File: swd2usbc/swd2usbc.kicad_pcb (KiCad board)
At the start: 4 copper layers, 18.3 x 16 mm, 16 parts, among them J1 USB_C_Receptacle_USB2.0, J2 Conn_ARM_JTAG_SWD_10, P1 USB_C_Plug, U1 ATtiny24-20M

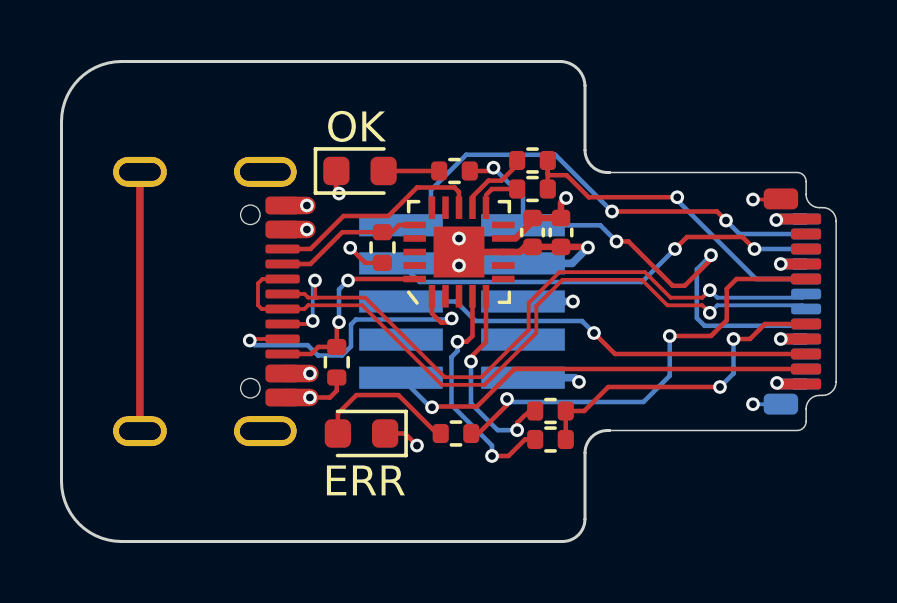
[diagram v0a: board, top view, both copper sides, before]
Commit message: Various fixes while ordering from JLCPCB
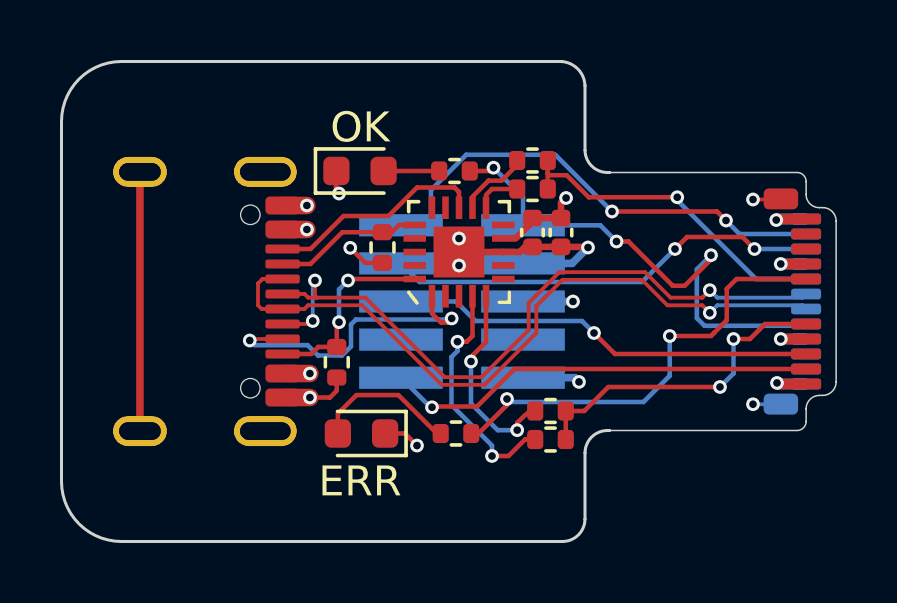
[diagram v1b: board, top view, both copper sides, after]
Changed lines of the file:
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@@
 	(generator_version "8.0")
 	(general
-		(thickness 0.8208)
+		(thickness 0.8)
 		(legacy_teardrops no)
 	)
@@
 			(layer "dielectric 1"
 				(type "prepreg")
-				(thickness 0.1 locked)
+				(thickness 0.1)
 				(material "FR408-HR")
 				(epsilon_r 3.69)
@@
 			(layer "dielectric 2"
 				(type "core")
-				(thickness 0.465)
+				(thickness 0.4442)
 				(material "FR408-HR")
 				(epsilon_r 3.69)
@@
 			(layer "dielectric 3"
 				(type "prepreg")
-				(thickness 0.1 locked)
+				(thickness 0.1)
 				(material "FR408-HR")
 				(epsilon_r 3.69)
@@
 			)
 		)
-		(property "LCSC" "C72043"
+		(property "LCSC" "C965804"
 			(at 0 0 0)
 			(unlocked yes)
@@
 			)
 		)
-		(property "LCSC" "C220282"
+		(property "LCSC" "C617902"
 			(at 0 0 0)
 			(layer "F.SilkS")
@@
 	)
 	(gr_text "ERR"
-		(at 165.35 73.5 0)
+		(at 165.2 73.5 0)
 		(layer "F.SilkS")
 		(effects
@@
 	)
 	(gr_text "OK"
-		(at 165.05 61.7 0)
+		(at 165.2 61.7 0)
 		(layer "F.SilkS")
 		(effects

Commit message: Should have checked my footprints...
USB-C plug footprint was incorrect. I had fixed it in the library but forgot to update it in the project.........
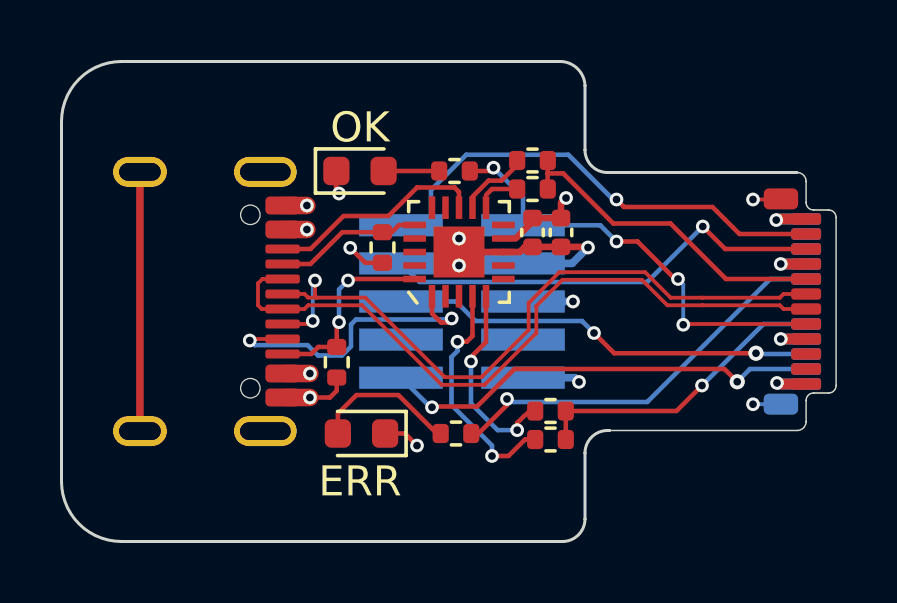
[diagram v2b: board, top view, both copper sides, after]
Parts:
- P1: moved to F.Cu
- turned P1 to -90 degrees
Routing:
- net /SBU1: track 16.7 -> 14.6 mm, vias 3 -> 4
- net /SBU2: track 14.6 -> 13.3 mm, vias 2 -> 1
- net /CC2: track 10.8 -> 10.2 mm, vias 2 -> 1
- net /NRST: track 14.4 -> 14.8 mm, vias 1 -> 2
- net /SWDCLK: track 14.5 -> 14.8 mm, vias 2 -> 1
- net /D-: track 23.7 -> 23.5 mm, vias 1 -> 0
- net /D+: track 24.2 -> 24.0 mm, vias 3 -> 2
- net /CC1: track 11.1 -> 11.0 mm, vias 1 -> 0
- net /SWO: vias 1 -> 2
- net /SWDIO: vias 2 -> 1

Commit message: Fixed some silkscreen and added OSWH logo
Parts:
- added REF**: OSHW-Symbol_6.7x6mm_SilkScreen, Symbol:OSHW-Symbol_6.7x6mm_SilkScreen, B.Cu at (175.9, 67.5)
